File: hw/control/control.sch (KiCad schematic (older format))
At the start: 5 parts

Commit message: [hw] Add LED bus driver
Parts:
- removed J?: DB9_Female_MountingHoles, symbol Connector:DB9_Female_MountingHoles
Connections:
- wire segments 42 -> 32
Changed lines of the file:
@@
 F4 "LED_EN0" O L 6200 2350 50
 F5 "LED_EN1" O L 6200 2450 50
-F6 "RS232_TX" O R 7500 3650 50
-F7 "RS232_RX" I R 7500 3550 50
 $EndSheet
 $Comp
@@
 	1    0    0    -1
 $EndComp
-$Comp
-L Connector:DB9_Female_MountingHoles J?
-U 1 1 6152356B
-P 9950 3700
-F 0 "J?" H 10130 3702 50  0000 L CNN
-F 1 "DB9_Female_MountingHoles" H 10130 3611 50  0000 L CNN
-F 2 "" H 9950 3700 50  0001 C CNN
-F 3 " ~" H 9950 3700 50  0001 C CNN
-	1    9950 3700
-	1    0    0    -1
-$EndComp
-Wire Wire Line
-	7500 3550 9550 3550
-Wire Wire Line
-	9550 3550 9550 3500
-Wire Wire Line
-	9550 3500 9650 3500
-Wire Wire Line
-	7500 3650 9550 3650
-Wire Wire Line
-	9550 3650 9550 3700
-Wire Wire Line
-	9550 3700 9650 3700
-$Comp
-L power:GND #PWR?
-U 1 1 61537FB3
-P 9550 4500
-F 0 "#PWR?" H 9550 4250 50  0001 C CNN
-F 1 "GND" H 9555 4327 50  0000 C CNN
-F 2 "" H 9550 4500 50  0001 C CNN
-F 3 "" H 9550 4500 50  0001 C CNN
-	1    9550 4500
-	1    0    0    -1
-$EndComp
-Wire Wire Line
-	9550 4100 9650 4100
-Wire Wire Line
-	9550 4100 9550 4300
-Wire Wire Line
-	9950 4300 9550 4300
 Wire Bus Line
 	5450 2300 5450 5300
 Wire Bus Line
 	5750 2550 5750 4650
-Connection ~ 9550 4300
-Wire Wire Line
-	9550 4300 9550 4500
 $EndSCHEMATC

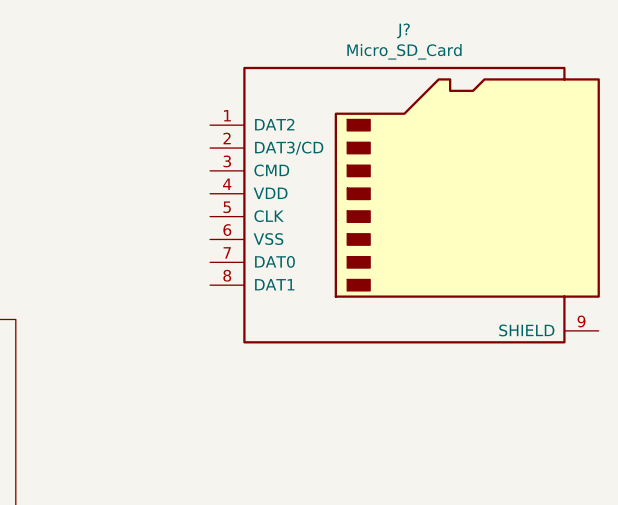
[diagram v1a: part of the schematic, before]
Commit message: [hw] Add secondary SD card connection
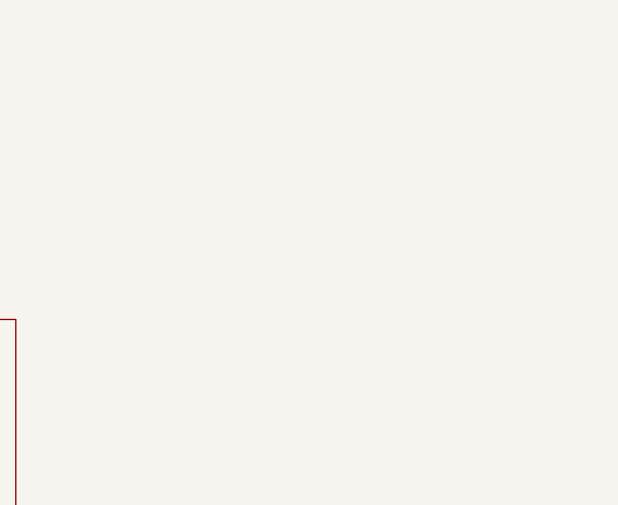
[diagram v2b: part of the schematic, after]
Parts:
- removed J?: Micro_SD_Card, symbol Connector:Micro_SD_Card
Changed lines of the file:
@@
 Wire Wire Line
 	4700 5000 7950 5000
-$Comp
-L Connector:Micro_SD_Card J?
-U 1 1 6151FF1A
-P 9250 1600
-F 0 "J?" H 9200 2317 50  0000 C CNN
-F 1 "Micro_SD_Card" H 9200 2226 50  0000 C CNN
-F 2 "" H 10400 1900 50  0001 C CNN
-F 3 "http://katalog.we-online.de/em/datasheet/693072010801.pdf" H 9250 1600 50  0001 C CNN
-	1    9250 1600
-	1    0    0    -1
-$EndComp
 Wire Bus Line
 	5450 2300 5450 5300

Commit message: [hw] Add annotations, minor fixes
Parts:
- removed J?: Barrel_Jack, symbol Connector:Barrel_Jack
- added J101: Screw_Terminal_01x02, symbol Connector:Screw_Terminal_01x02
- gave numbers to parts that had none: 2
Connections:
- wire segments 32 -> 36
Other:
- moved on the sheet: J102, J103

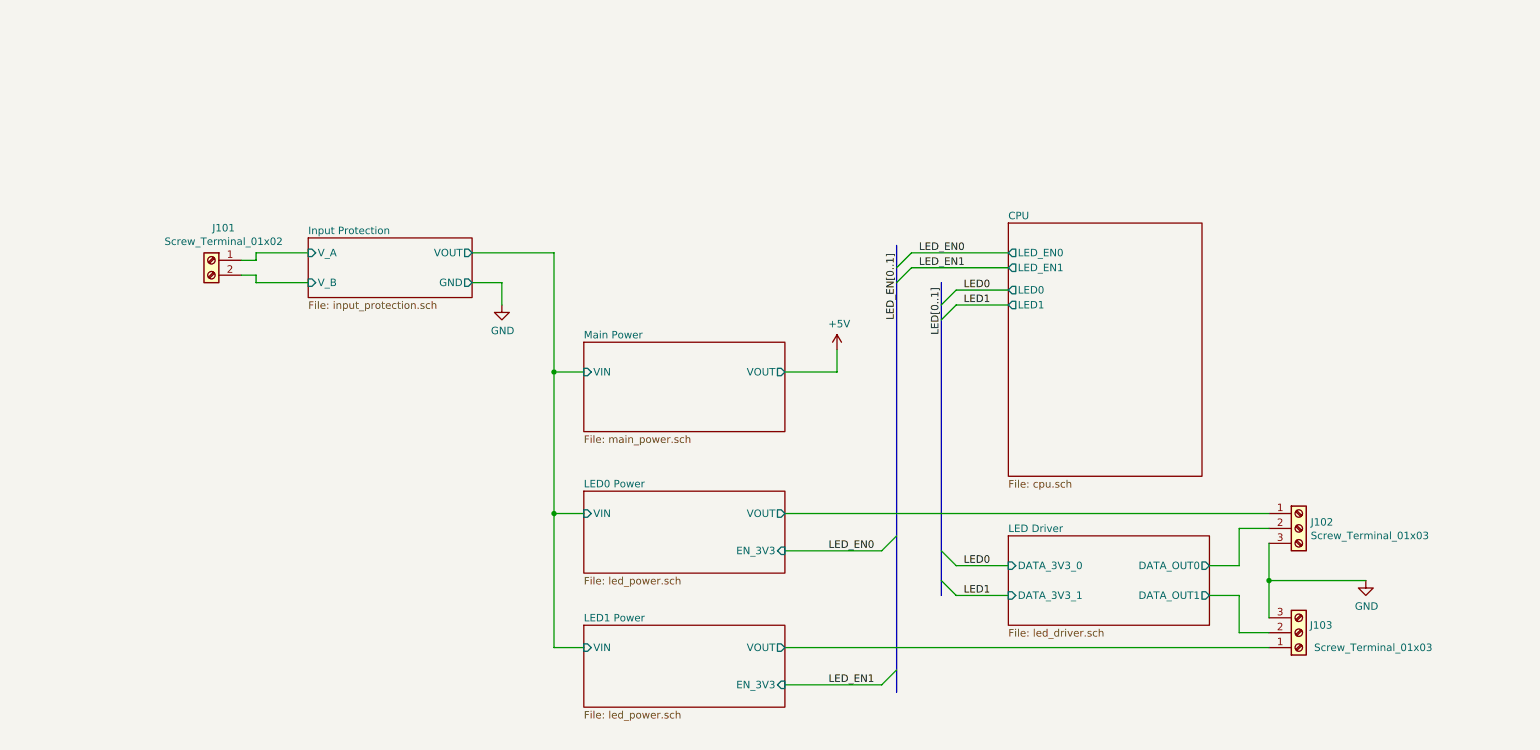
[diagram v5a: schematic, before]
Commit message: [hw] Add alternative LED data line from SPI
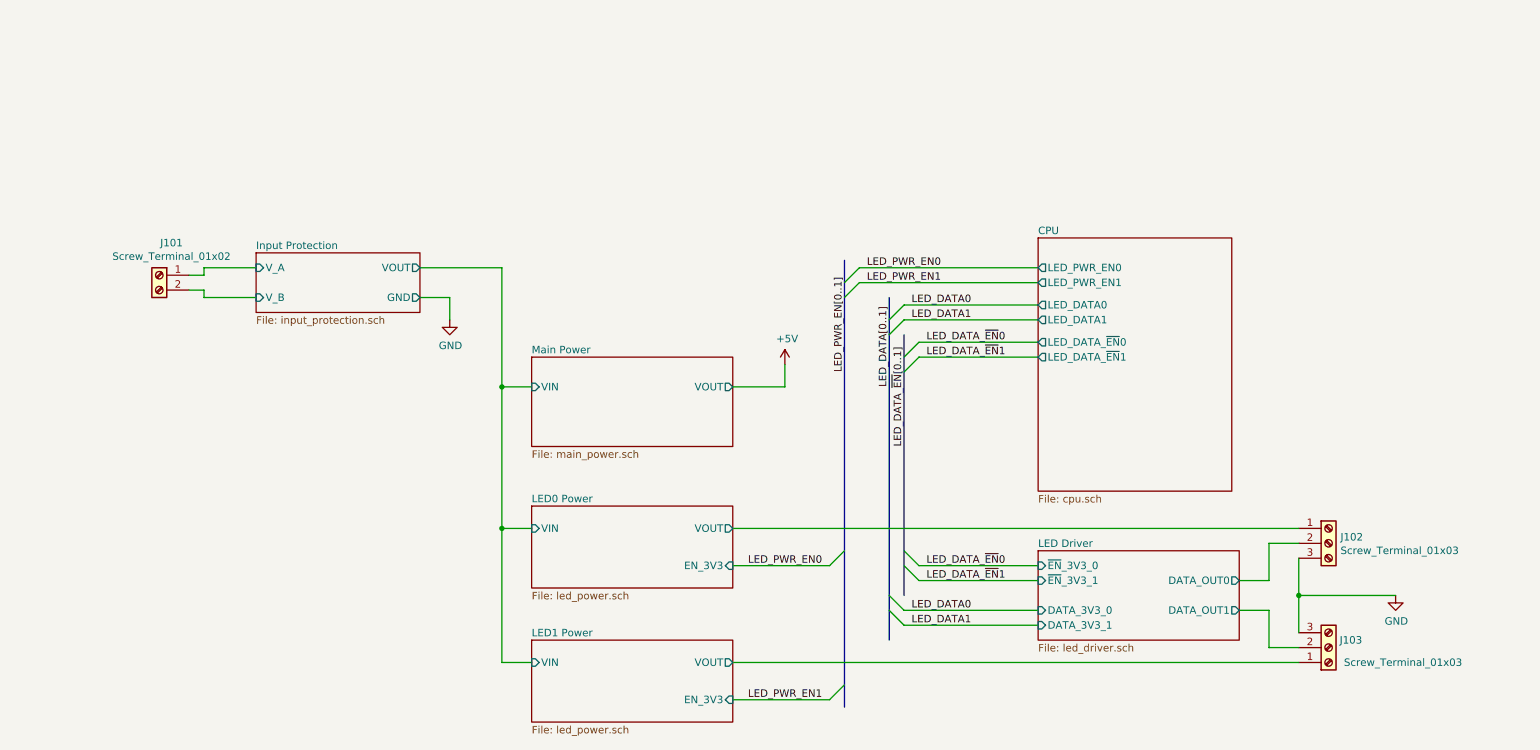
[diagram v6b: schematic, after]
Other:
- moved on the sheet: J101, J102, J103

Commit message: [hw] Assign most of the controller footprints
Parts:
- J101: footprint (none) -> TerminalBlock_Phoenix:TerminalBlock_Phoenix_MKDS-1,5-2_1x02_P5.00mm_Horizontal
- J102, J103: footprint (none) -> TerminalBlock_Phoenix:TerminalBlock_Phoenix_MKDS-1,5-3_1x03_P5.00mm_Horizontal
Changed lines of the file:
@@
 F 0 "J102" H 9280 4442 50  0000 L CNN
 F 1 "Screw_Terminal_01x03" H 9280 4351 50  0000 L CNN
-F 2 "" H 9200 4400 50  0001 C CNN
+F 2 "TerminalBlock_Phoenix:TerminalBlock_Phoenix_MKDS-1,5-3_1x03_P5.00mm_Horizontal" H 9200 4400 50  0001 C CNN
 F 3 "~" H 9200 4400 50  0001 C CNN
 	1    9200 4400
@@
 F 0 "J103" H 9350 5050 50  0000 C CNN
 F 1 "Screw_Terminal_01x03" H 9700 5200 50  0000 C CNN
-F 2 "" H 9200 5100 50  0001 C CNN
+F 2 "TerminalBlock_Phoenix:TerminalBlock_Phoenix_MKDS-1,5-3_1x03_P5.00mm_Horizontal" H 9200 5100 50  0001 C CNN
 F 3 "~" H 9200 5100 50  0001 C CNN
 	1    9200 5100
@@
 F 0 "J101" H 1268 2817 50  0000 C CNN
 F 1 "Screw_Terminal_01x02" H 1268 2726 50  0000 C CNN
-F 2 "" H 1350 2600 50  0001 C CNN
+F 2 "TerminalBlock_Phoenix:TerminalBlock_Phoenix_MKDS-1,5-2_1x02_P5.00mm_Horizontal" H 1350 2600 50  0001 C CNN
 F 3 "~" H 1350 2600 50  0001 C CNN
 	1    1350 2600

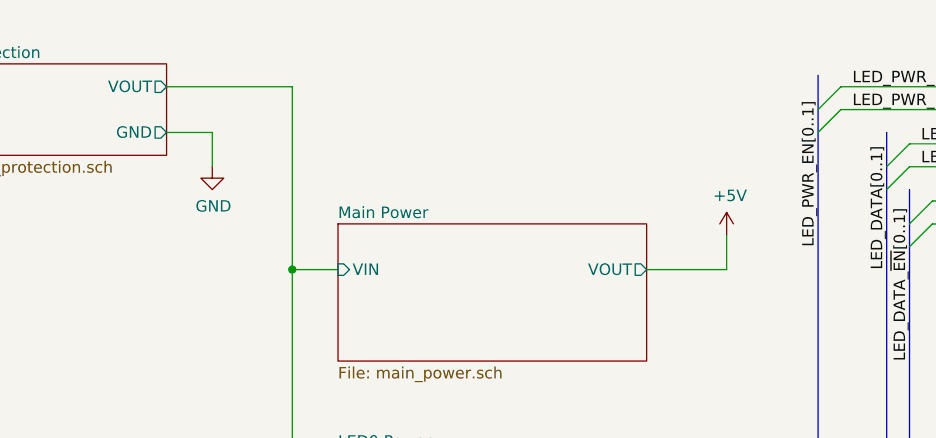
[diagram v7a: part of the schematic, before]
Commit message: [hw] Assign control board footprints
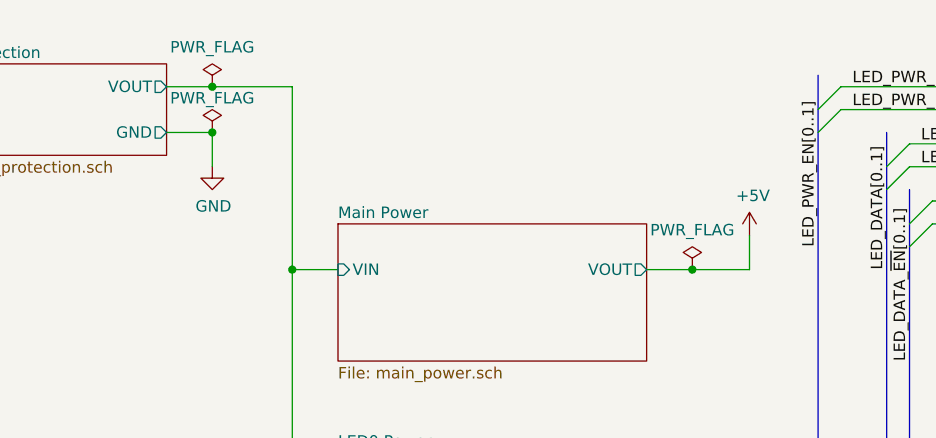
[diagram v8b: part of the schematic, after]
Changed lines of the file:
@@
 L power:+5V #PWR0102
 U 1 1 614A9497
-P 5550 3200
-F 0 "#PWR0102" H 5550 3050 50  0001 C CNN
-F 1 "+5V" H 5565 3373 50  0000 C CNN
-F 2 "" H 5550 3200 50  0001 C CNN
-F 3 "" H 5550 3200 50  0001 C CNN
-	1    5550 3200
+P 5650 3200
+F 0 "#PWR0102" H 5650 3050 50  0001 C CNN
+F 1 "+5V" H 5665 3373 50  0000 C CNN
+F 2 "" H 5650 3200 50  0001 C CNN
+F 3 "" H 5650 3200 50  0001 C CNN
+	1    5650 3200
 	1    0    0    -1
 $EndComp
@@
 	3650 3350 3650 2550
 Wire Wire Line
-	3650 2550 3100 2550
+	3650 2550 3300 2550
 Connection ~ 3650 3350
 Entry Wire Line
@@
 	1650 2600 1550 2600
 Wire Wire Line
-	1650 2550 2000 2550
-Wire Wire Line
 	1650 2750 1650 2700
 Wire Wire Line
 	1650 2700 1550 2700
 Wire Wire Line
-	1650 2750 2000 2750
-Wire Wire Line
-	5550 3350 5550 3200
-Wire Wire Line
-	5200 3350 5550 3350
+	5650 3350 5650 3200
+Wire Wire Line
+	5200 3350 5400 3350
 Wire Wire Line
 	6350 4950 7250 4950
@@
 Text Label 6500 4650 0    50   ~ 0
 LED_DATA_~EN~1
+$Comp
+L power:PWR_FLAG #FLG0103
+U 1 1 61664238
+P 5400 3350
+F 0 "#FLG0103" H 5400 3425 50  0001 C CNN
+F 1 "PWR_FLAG" H 5400 3523 50  0000 C CNN
+F 2 "" H 5400 3350 50  0001 C CNN
+F 3 "~" H 5400 3350 50  0001 C CNN
+	1    5400 3350
+	1    0    0    -1
+$EndComp
+Connection ~ 5400 3350
+Wire Wire Line
+	5400 3350 5650 3350
+$Comp
+L power:PWR_FLAG #FLG0102
+U 1 1 61668437
+P 3300 2750
+F 0 "#FLG0102" H 3300 2825 50  0001 C CNN
+F 1 "PWR_FLAG" H 3300 2900 50  0000 C CNN
+F 2 "" H 3300 2750 50  0001 C CNN
+F 3 "~" H 3300 2750 50  0001 C CNN
+	1    3300 2750
+	1    0    0    -1
+$EndComp
+Connection ~ 3300 2750
+Wire Wire Line
+	1650 2750 2000 2750
+Wire Wire Line
+	1650 2550 2000 2550
+$Comp
+L power:PWR_FLAG #FLG0101
+U 1 1 6166B01E
+P 3300 2550
+F 0 "#FLG0101" H 3300 2625 50  0001 C CNN
+F 1 "PWR_FLAG" H 3300 2723 50  0000 C CNN
+F 2 "" H 3300 2550 50  0001 C CNN
+F 3 "~" H 3300 2550 50  0001 C CNN
+	1    3300 2550
+	1    0    0    -1
+$EndComp
+Connection ~ 3300 2550
+Wire Wire Line
+	3300 2550 3100 2550
 Wire Bus Line
 	6350 3000 6350 4750
